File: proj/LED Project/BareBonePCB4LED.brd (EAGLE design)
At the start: 160 x 100 mm, 12 parts, among them J3 AVR_SPI_PROG_3X2NS, Y1 16MHz

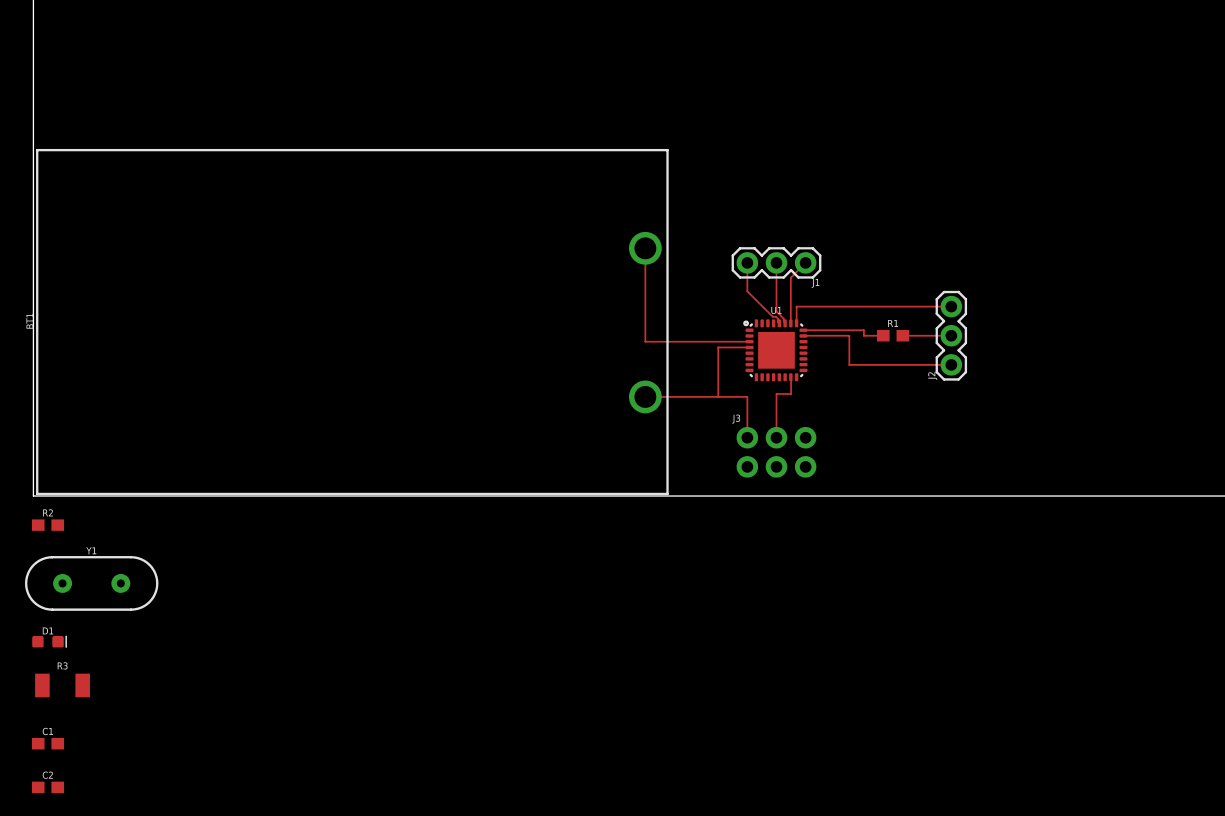
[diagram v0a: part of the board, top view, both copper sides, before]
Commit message: Added volt regulator to bring battery from 9v to 5v for board tests
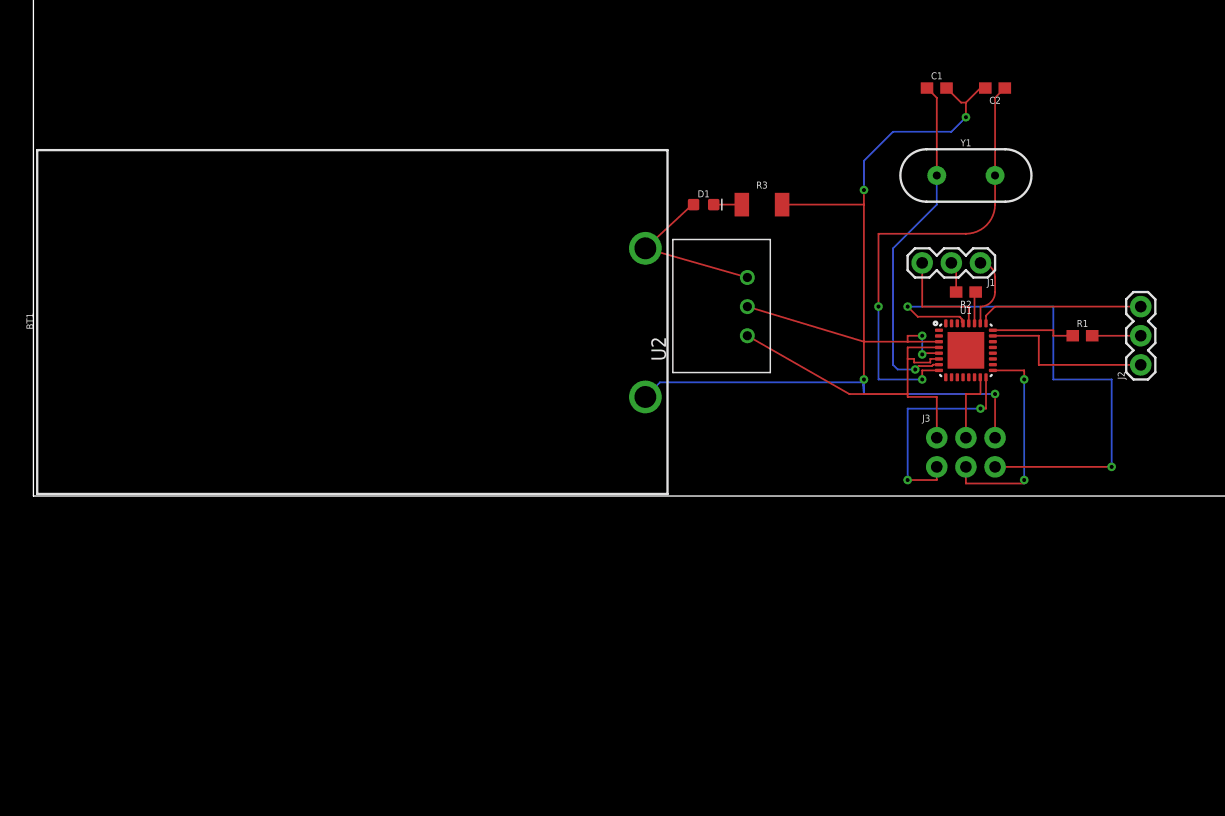
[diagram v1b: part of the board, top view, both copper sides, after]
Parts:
- added U2: R-78E5.0-1.0, SparkFun-IC-Power:DC-DC_CONVERTER_78XX
- moved C2 102.6 mm to (83.8, 35.6), turned to 180 degrees
- moved C1 96.3 mm to (78.7, 35.6)
- moved Y1 84.1 mm to (81.3, 27.9)
- moved R2 82.5 mm to (81.3, 17.8), turned to 180 degrees
- moved R3 74.0 mm to (63.5, 25.4)
- moved D1 68.7 mm to (58.4, 25.4)
- moved J3 16.5 mm to (81.3, 3.81)
- moved U1 16.5 mm to (81.3, 12.7)
- moved J2 16.5 mm to (96.5, 11.4)
- moved R1 16.5 mm to (91.4, 14.0)
- moved J1 15.2 mm to (82.5, 20.3)
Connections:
- removed net N$15: U1.29
- new net 9V: BT1.+, D1.A, U2.VOUT
- net GND: now also BT1.-, U2.GND; no longer BT1.+
- net RST: now also U1.29
- net VCC: now also U2.VIN; no longer BT1.-, D1.A
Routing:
- net GND: track 17.2 -> 101.5 mm, vias 0 -> 6
- net RST: track 0.00 -> 47.5 mm, vias 0 -> 2
- net N$12: track 0.00 -> 40.5 mm, vias 0 -> 2
- net N$11: track 0.00 -> 30.4 mm, vias 0 -> 1
- net MISO: track 0.00 -> 19.5 mm, vias 0 -> 2
- net SCK: track 0.00 -> 19.1 mm, vias 0 -> 2
- net 9V: track 0.00 -> 14.9 mm
- net VCC: track 19.5 -> 31.8 mm
- net N$8: track 0.00 -> 2.83 mm
- net N$6: track 6.59 -> 9.33 mm
- net N$5: track 5.41 -> 2.96 mm
- net N$10: track 0.00 -> 2.45 mm
- net N$4: track 5.80 -> 6.33 mm

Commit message: Making the PCB pretty
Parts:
- removed BT1: (no value), SparkFun-Batteries:BATTCON_9V
- removed J1, J2: (no value), SparkFun-Connectors:1X03
- removed U2: R-78E5.0-1.0, SparkFun-IC-Power:DC-DC_CONVERTER_78XX
- added BAT: (no value), SparkFun-Batteries:BATTCON_9V
- added NP1, NP2: (no value), SparkFun-Connectors:1X03
- added VR: R-78E5.0-1.0, SparkFun-IC-Power:DC-DC_CONVERTER_78XX
- moved C2 33.7 mm to (72.4, 3.81)
- moved C1 33.3 mm to (68.6, 3.81)
- moved Y1 22.2 mm to (69.8, 8.89)
- moved R1 12.5 mm to (80.0, 19.1)
- moved R2 11.7 mm to (72.4, 25.4), turned to 90 degrees
- moved U1 10.2 mm to (72.4, 17.8)
- moved J3 6.35 mm to (81.3, 10.2)
- moved D1 2.54 mm to (55.9, 25.4)
- moved R3 2.54 mm to (61.0, 25.4)
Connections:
- removed net N$1: J2.1, U1.23
- removed net N$3: J2.3, U1.25
- removed net N$4: J1.1, U1.26
- removed net N$6: J1.3, U1.28
- net 9V: now also BAT.+, VR.VOUT; no longer BT1.+, U2.VOUT
- net GND: now also BAT.-, NP1.1, NP2.1, VR.GND; no longer BT1.-, U2.GND
- net N$2: now also NP1.2; no longer J2.2
- net N$5: now also NP2.2; no longer J1.2
- net VCC: now also NP1.3, NP2.3, VR.VIN; no longer U2.VIN
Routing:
- net GND: track 101.5 -> 0.00 mm, vias 6 -> 0
- net VCC: track 31.8 -> 1.40 mm
- net N$12: track 40.5 -> 15.0 mm, vias 2 -> 0
- net RST: track 47.5 -> 26.8 mm, vias 2 -> 1
- net N$11: track 30.4 -> 14.3 mm, vias 1 -> 0
- net N$1: track 15.5 -> 0.00 mm
- net N$3: track 14.5 -> 0.00 mm
- net MISO: track 19.5 -> 8.45 mm, vias 2 -> 0
- net N$6: track 9.33 -> 0.00 mm
- net SCK: track 19.1 -> 11.0 mm, vias 2 -> 0
- net N$4: track 6.33 -> 0.00 mm
- net MOSI: track 6.56 -> 11.9 mm, vias 0 -> 1
- net N$7: track 7.44 -> 4.64 mm
- net N$8: track 2.83 -> 4.73 mm
- net 9V: track 14.9 -> 13.4 mm
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- added copper zone on layer 16, net GND
- added copper zone on layer 1, net VCC
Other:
- board text added: "GND"
- board text added: "MOSI"
- board text added: "PWR"

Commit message: Update proj/LED Project/BareBonePCB4LED.brd
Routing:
- net VCC: track 1.40 -> 50.0 mm, vias 0 -> 2
- net GND: track 0.00 -> 9.72 mm, vias 0 -> 3
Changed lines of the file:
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@@
 <vertex x="50.8" y="1.27"/>
 </polygon>
+<wire x1="70.04" y1="17.53" x2="67.441" y2="17.53" width="0.35" layer="1"/>
+<wire x1="67.441" y1="17.53" x2="67.437" y2="17.526" width="0.35" layer="1"/>
+<via x="67.437" y="17.526" extent="1-16" drill="0.35"/>
+<wire x1="62.715" y1="25.4" x2="64.77" y2="25.4" width="0.35" layer="1"/>
+<via x="64.77" y="25.4" extent="1-16" drill="0.35"/>
+<wire x1="69.43" y1="3.81" x2="69.43" y2="5.041" width="0.35" layer="1"/>
+<wire x1="69.43" y1="5.041" x2="70.104" y2="5.715" width="0.35" layer="1"/>
+<wire x1="70.104" y1="5.715" x2="70.358" y2="5.715" width="0.35" layer="1"/>
+<via x="70.358" y="5.715" extent="1-16" drill="0.35"/>
+<wire x1="71.54" y1="3.81" x2="71.54" y2="4.914" width="0.35" layer="1"/>
+<wire x1="70.739" y1="5.715" x2="70.358" y2="5.715" width="0.35" layer="1"/>
+<wire x1="71.54" y1="4.914" x2="70.739" y2="5.715" width="0.35" layer="1"/>
 <wire x1="70.04" y1="17.53" x2="70.04" y2="18.53" width="0" layer="19" extent="1-1"/>
-<wire x1="62.23" y1="17.78" x2="70.04" y2="17.53" width="0" layer="19" extent="1-1"/>
-<wire x1="62.715" y1="25.4" x2="62.23" y2="17.78" width="0" layer="19" extent="1-1"/>
-<wire x1="69.43" y1="3.81" x2="70.04" y2="17.53" width="0" layer="19" extent="1-1"/>
-<wire x1="71.54" y1="3.81" x2="69.43" y2="3.81" width="0" layer="19" extent="1-1"/>
 </signal>
 <signal name="VCC">
@@
 <wire x1="70.04" y1="17.03" x2="69.354" y2="17.03" width="0.3048" layer="1"/>
 <wire x1="69.354" y1="17.03" x2="69.342" y2="17.018" width="0.3048" layer="1"/>
-<wire x1="70.04" y1="18.03" x2="70.036" y2="18.034" width="0.3048" layer="1"/>
-<wire x1="70.036" y1="18.034" x2="69.342" y2="18.034" width="0.3048" layer="1"/>
-<wire x1="78.74" y1="11.43" x2="70.04" y2="17.03" width="0" layer="19" extent="1-1"/>
+<wire x1="78.74" y1="11.43" x2="76.2" y2="13.97" width="0.1524" layer="1"/>
+<via x="76.2" y="13.97" extent="1-16" drill="0.35"/>
+<wire x1="76.2" y1="13.97" x2="71.12" y2="13.97" width="0.1524" layer="16"/>
+<via x="71.12" y="13.97" extent="1-16" drill="0.35"/>
+<wire x1="71.12" y1="13.97" x2="70.04" y2="15.05" width="0.35" layer="1"/>
+<wire x1="74.1174" y1="3.1743875" x2="73.9256125" y2="2.9826" width="0.35" layer="1"/>
+<wire x1="70.04" y1="17.0276" x2="70.0198" y2="17.0074" width="0.35" layer="1"/>
+<wire x1="70.04" y1="15.05" x2="70.04" y2="13.02561875" width="0.35" layer="1"/>
+<wire x1="73.9256125" y1="2.9826" x2="67.0443875" y2="2.9826" width="0.35" layer="1"/>
+<wire x1="67.0443875" y1="2.9826" x2="66.1571" y2="3.8698875" width="0.35" layer="1"/>
+<wire x1="66.1571" y1="3.8698875" x2="66.1571" y2="13.71371875" width="0.35" layer="1"/>
+<wire x1="66.1571" y1="13.71371875" x2="69.45078125" y2="17.0074" width="0.35" layer="1"/>
+<wire x1="69.45078125" y1="17.0074" x2="70.0198" y2="17.0074" width="0.35" layer="1"/>
+<wire x1="70.04" y1="13.02561875" x2="74.1174" y2="8.94821875" width="0.35" layer="1"/>
+<wire x1="74.1174" y1="8.94821875" x2="74.1174" y2="3.1743875" width="0.35" layer="1"/>
+<wire x1="70.04" y1="17.03" x2="68.719" y2="17.03" width="0.35" layer="1"/>
+<wire x1="68.719" y1="17.03" x2="68.707" y2="17.018" width="0.35" layer="1"/>
+<wire x1="69.85" y1="18.034" x2="69.342" y2="18.034" width="0.35" layer="1"/>
+<wire x1="69.85" y1="18.034" x2="70.036" y2="18.034" width="0.35" layer="1"/>
+<wire x1="70.036" y1="18.034" x2="70.0376" y2="18.0324" width="0.35" layer="1"/>
+<wire x1="70.0376" y1="18.0324" x2="70.04" y2="18.0324" width="0.35" layer="1"/>
+<wire x1="70.036" y1="18.034" x2="70.04" y2="18.03" width="0" layer="19" extent="1-1"/>
+<wire x1="70.04" y1="17.0276" x2="70.04" y2="18.03" width="0" layer="19" extent="1-1"/>
 </signal>
 <signal name="N$2">
@@
 <mfgpreviewcolor name="substratecolor" color="0xFF786E46"/>
 </mfgpreviewcolors>
+<errors>
+</errors>
 </board>
 </drawing>

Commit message: fixes
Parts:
- removed VR: R-78E5.0-1.0, SparkFun-IC-Power:DC-DC_CONVERTER_78XX
- added C3: 1mF, SparkFun-Capacitors:CPOL-RADIAL-5MM-10MM
- added R4: 400, SparkFun-Resistors:0603
- added S1: MOMENTARY-SWITCH-SPST-PTH-6.0MM-KIT, SparkFun-Switches:TACTILE_SWITCH_PTH_6.0MM_KIT
- added U2: (no value), SparkFun-IC-Microcontroller:MLF32-PAD
- R1: value 470 -> 83
- R2: value 470 -> 10k
- R3: value 500 -> 400; device SparkFun-Resistors:1210 -> SparkFun-Resistors:0603
- U1: value (none) -> R-78E5.0-1.0; device SparkFun-IC-Microcontroller:MLF32-PAD -> SparkFun-IC-Power:DC-DC_CONVERTER_78XX
- moved R1 20.1 mm to (61.0, 25.4)
- moved R3 20.1 mm to (80.0, 19.1)
- moved U1 10.2 mm to (62.2, 17.8), turned to 90 degrees
- moved R2 4.02 mm to (68.6, 24.1), turned to 0 degrees
- renumbered BAT to BT1, NP1 to J2, NP2 to J1
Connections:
- removed net N$11: C1.1, U1.7, Y1.1
- removed net N$12: C2.1, U1.8, Y1.2
- removed net N$2: J2.2, R1.2
- removed net N$5: J1.2, R2.2
- removed net N$8: R2.1, U1.27
- new net DATA: R4.1, U2.27
- new net DATA1: J2.2, R3.2
- new net DATA2: J1.2, R4.2
- new net XTAL1: C1.1, U2.7, Y1.1
- new net XTAL2: C2.1, U2.8, Y1.2
- net 9V: now also U1.VOUT; no longer D1.A, VR.VOUT
- net GND: now also C3.-, R1.2, S1.3, U1.GND, U2.3, U2.5, U2.PAD; no longer R3.2, U1.3, U1.5, VR.GND
- net MISO: now also U2.16; no longer U1.16
- net MOSI: now also U2.15; no longer U1.15
- net N$10: now also R1.1; no longer R3.1
- net N$7: now also R3.1, U2.24; no longer R1.1, U1.24
- net RST: now also R2.2, S1.1, U2.29; no longer U1.29
- net RX: now also U2.30; no longer U1.30
- net SCK: now also U2.17; no longer U1.17
- net TX: now also U2.31; no longer U1.31
- net VCC: now also C3.+, D1.A, R2.1, U1.VIN, U2.18, U2.4, U2.6; no longer U1.4, U1.6, VR.VIN
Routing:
- net XTAL2: track 0.00 -> 15.0 mm
- net N$12: track 15.0 -> 0.00 mm
- net XTAL1: track 0.00 -> 14.3 mm
- net N$11: track 14.3 -> 0.00 mm
- net RST: track 26.8 -> 39.8 mm
- net VCC: track 50.0 -> 44.4 mm
- net GND: track 9.72 -> 14.5 mm
- net N$8: track 4.73 -> 0.00 mm
- net DATA: track 0.00 -> 4.73 mm
- net 9V: track 13.4 -> 9.94 mm
- net N$5: track 2.96 -> 0.00 mm
- net DATA2: track 0.00 -> 2.96 mm
- net N$2: track 2.96 -> 0.00 mm
- net DATA1: track 0.00 -> 2.96 mm
- net N$10: track 2.45 -> 3.35 mm
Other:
- board size 160 x 100 mm -> 58.4 x 32.7 mm

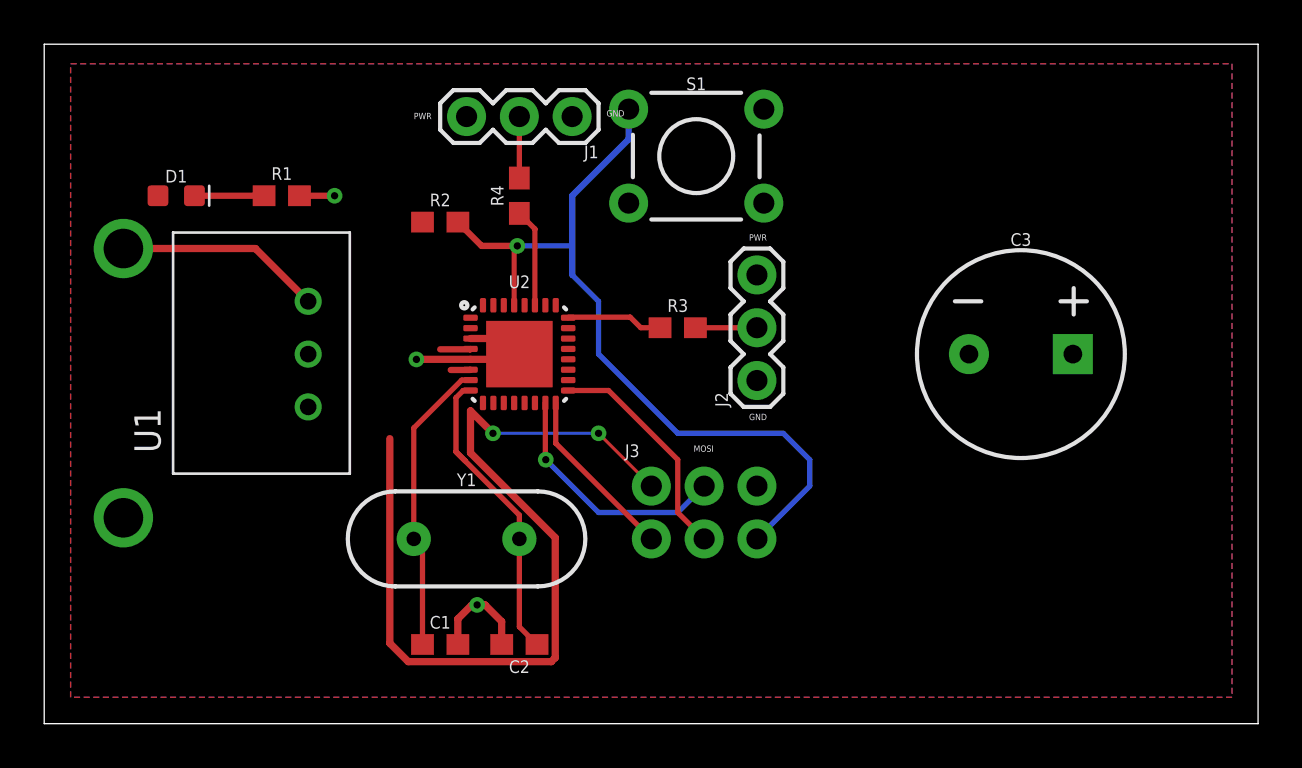
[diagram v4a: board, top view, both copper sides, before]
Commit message: Cleaning LED Schematic + Board
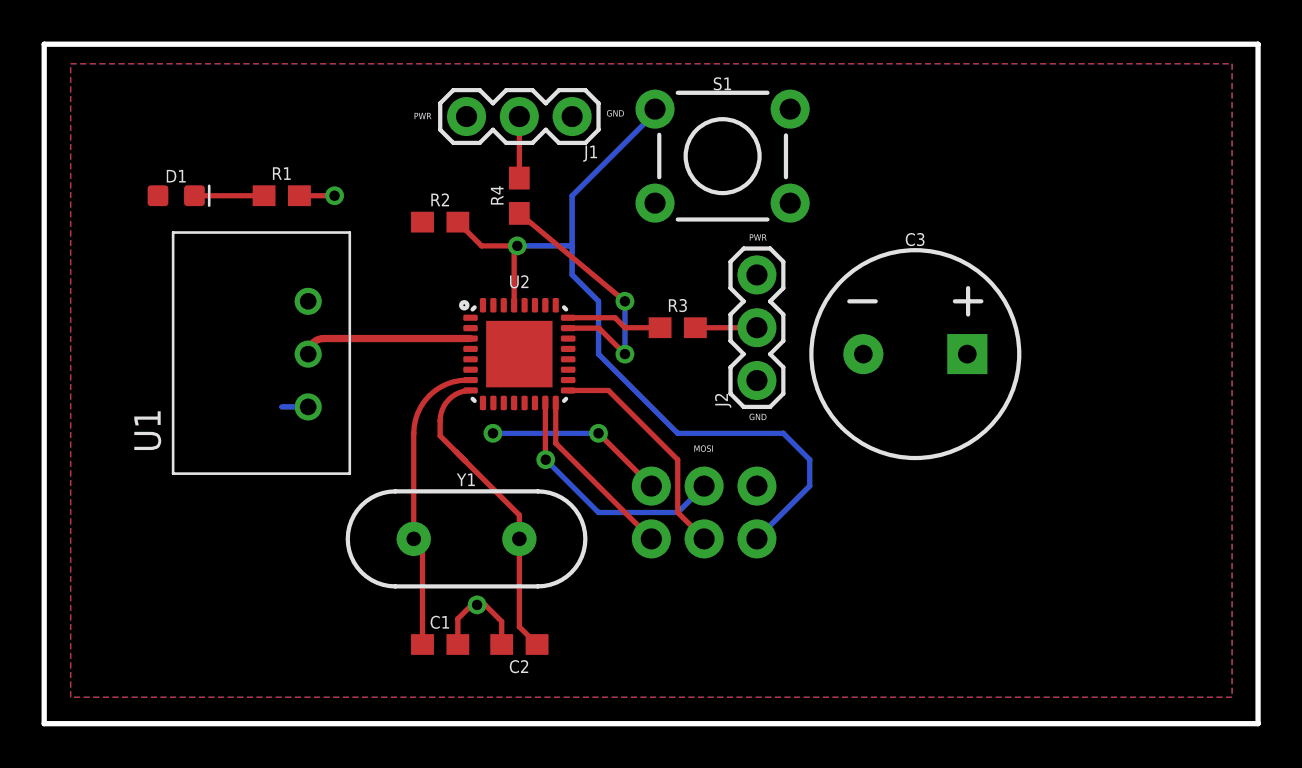
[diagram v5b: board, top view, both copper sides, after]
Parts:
- removed BT1: (no value), SparkFun-Batteries:BATTCON_9V
- moved C3 5.08 mm to (91.4, 17.8)
- moved S1 1.27 mm to (82.2, 27.3)
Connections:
- net N$7 renamed NP2
- removed net DATA: R4.1, U2.27
- new net NP1: R4.1, U2.23
- net 9V: now also U1.VIN; no longer BT1.+, U1.VOUT
- net DATA1: now also J1.2, R4.2; no longer J2.2, R3.2
- net DATA2: now also J2.2, R3.2; no longer J1.2, R4.2
- net GND: no longer BT1.-, U2.5, U2.PAD
- net VCC: now also U1.VOUT; no longer U1.VIN
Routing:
- net VCC: track 44.4 -> 8.67 mm
- net NP1: track 0.00 -> 12.4 mm, vias 0 -> 2
- net 9V: track 9.94 -> 1.27 mm
- net DATA: track 4.73 -> 0.00 mm
- net XTAL2: track 15.0 -> 16.0 mm
- net GND: track 14.5 -> 15.4 mm, vias 3 -> 2
